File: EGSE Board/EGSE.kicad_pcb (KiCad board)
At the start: 2 copper layers, 149.9 x 112.8 mm, 51 parts, among them J1 DC37_Receptacle, U1 VOR2121A8, U11 DAC121S101, U12 LD1117S33TR_SOT223, U2 VOR2121A8, U3 INA3221, U4 INA238AQDGSRQ1, U5 MAX31865xAP, U6 ISU0205S15, U7 ISO1540, U8 OPA551P, U9 LD1117S33TR_SOT223

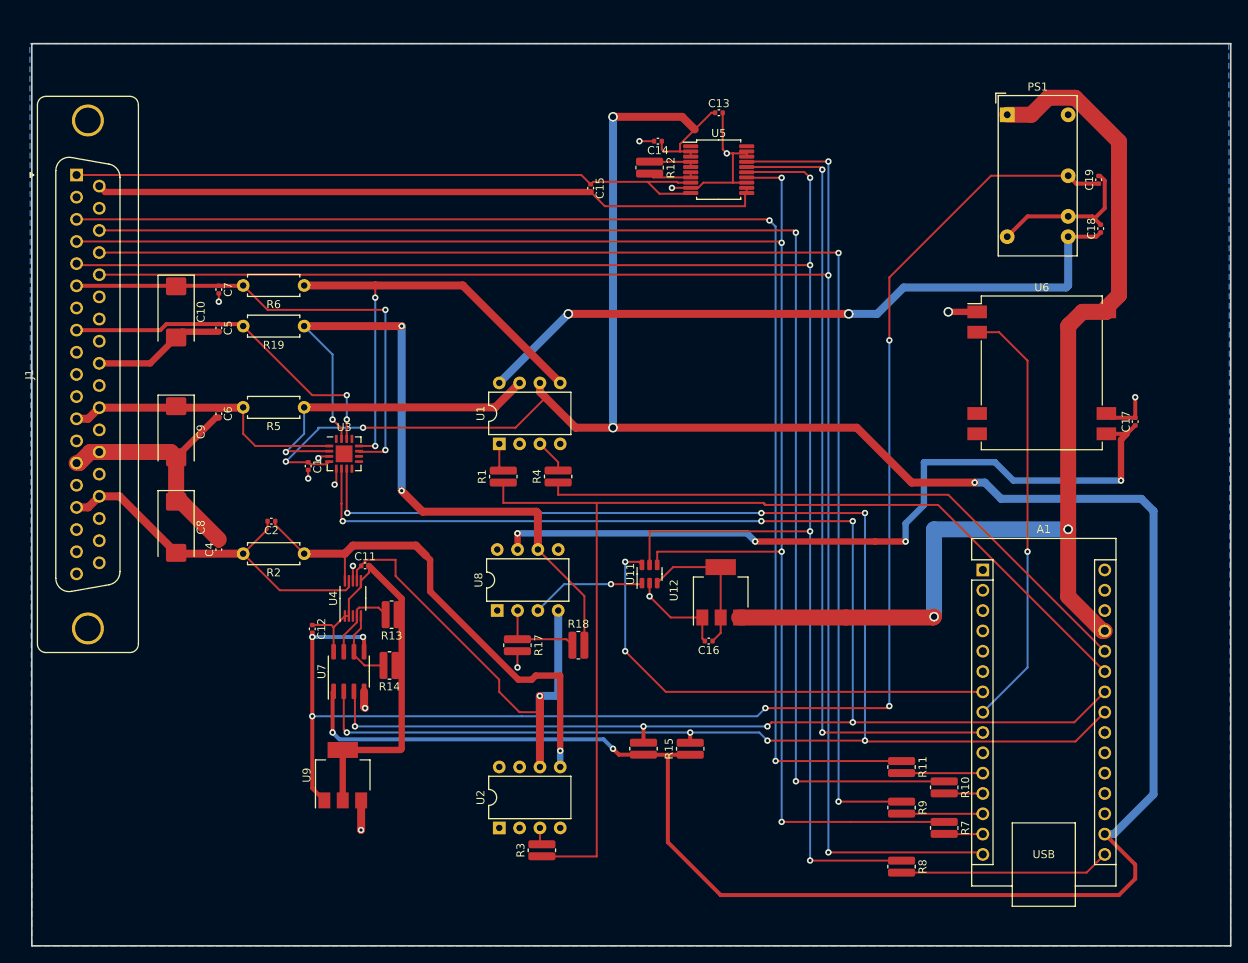
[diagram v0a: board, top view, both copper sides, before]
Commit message: Regular update
Created Gerber files for production
Changed names in arduino code to reflect signal names used by MSSL and on EGSE board
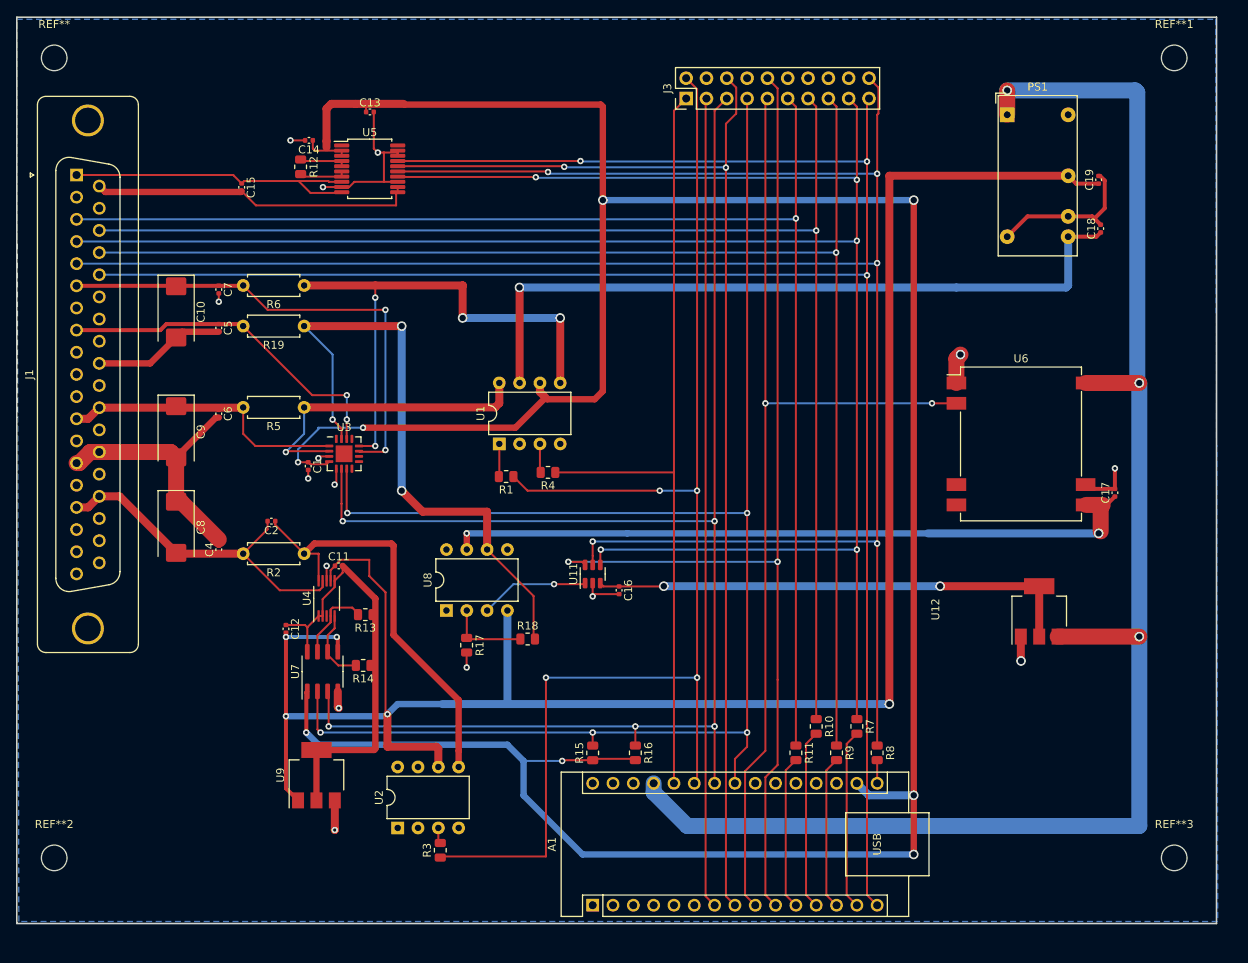
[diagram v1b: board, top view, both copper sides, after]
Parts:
- added J3: Conn_02x10_Odd_Even, Connector_PinHeader_2.54mm:PinHeader_2x10_P2.54mm_Vertical, F.Cu at (103.1, 45.5)
- added REF**: MountingHole_3.2mm_M3, MountingHole:MountingHole_3.2mm_M3, F.Cu at (24.1, 40.4)
- added REF**1: MountingHole_3.2mm_M3, MountingHole:MountingHole_3.2mm_M3, F.Cu at (164.1, 40.4)
- added REF**2: MountingHole_3.2mm_M3, MountingHole:MountingHole_3.2mm_M3, F.Cu at (24.1, 140.4)
- added REF**3: MountingHole_3.2mm_M3, MountingHole:MountingHole_3.2mm_M3, F.Cu at (164.1, 140.4)
- R1, R10, R11, R12, R13, R14, R15, R16, R17, R18, R3, R4, R7, R8, R9: footprint Resistor_SMD:R_0612_1632Metric -> Resistor_SMD:R_0805_2012Metric
- moved A1 64.3 mm to (91.4, 146.3), turned to 90 degrees
- moved C15 43.6 mm to (47.6, 56.6)
- moved R12 43.6 mm to (54.9, 54.0)
- moved C14 43.6 mm to (56.0, 50.7)
- moved U5 43.6 mm to (63.6, 54.3)
- moved C13 43.6 mm to (63.6, 47.1)
- moved U12 39.9 mm to (147.3, 109.6)
- moved R10 17.7 mm to (119.4, 124.0)
- moved R7 16.7 mm to (124.5, 124.0)
- moved R8 14.5 mm to (127.0, 127.3)
- moved R11 13.3 mm to (116.8, 127.3)
- moved C16 12.9 mm to (94.7, 106.9), turned to -90 degrees
- moved R3 12.7 mm to (72.4, 139.4)
- moved U2 12.7 mm to (67.1, 136.6)
- moved R15 12.2 mm to (91.4, 127.3)
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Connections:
- A1 pad 10: /TRIG -> /HTR_DAC_CS
- A1 pad 7: /HTR_DAC_CS -> /TRIG
- A1 pad 8: /HTR_EN -> /RTD_MON_CS
- A1 pad 9: /RTD_MON_CS -> /HTR_EN
- C18 pad 1: Net-(PS1-+Vout) -> /PowerSupplies/+12V_Unswitched
- PS1 pad 6: Net-(PS1-+Vout) -> /PowerSupplies/+12V_Unswitched
- R5 pad 1: Net-(U1-S1') -> Net-(U1-S1)
- U1 pad 7: Net-(U1-S1') -> /PowerSupplies/+12V_Unswitched
- U1 pad 8: Net-(PS1-+Vout) -> Net-(U1-S1)
- U3 pad 2: Net-(U1-S1') -> Net-(U1-S1)
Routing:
- net /TRIG: track 0.00 -> 101.3 mm
- net /PowerSupplies/+12V_Unswitched: track 0.00 -> 91.0 mm, vias 0 -> 1
- net Net-(PS1-+Vout): track 86.5 -> 0.00 mm, vias 2 -> 0
- net /HTR_DAC_CS: track 60.2 -> 133.5 mm
- net /HTR_EN: track 54.0 -> 126.4 mm, vias 1 -> 2
- net /DETEC_SCK: track 221.1 -> 282.7 mm, vias 4 -> 5
- net /DETEC_MOSI: track 210.6 -> 267.1 mm, vias 4 -> 5
- net +5V: track 136.8 -> 191.9 mm, vias 2 -> 3
- net /DETEC_MISO: track 207.1 -> 256.2 mm
- net /RTD_MON_CS: track 100.0 -> 146.0 mm
- net /DETEC_TRP: track 83.5 -> 39.8 mm
- net /DETEC_TRP_RTN: track 84.1 -> 40.6 mm
- net Net-(U11B-+V_A): track 18.4 -> 61.3 mm, vias 0 -> 2
- net Net-(U1-S1'): track 40.2 -> 0.00 mm, vias 1 -> 0
- net Net-(U1-S1): track 0.00 -> 39.1 mm, vias 0 -> 1
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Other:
- board size 149.9 x 112.8 mm -> 150 x 113.3 mm

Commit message: PCB Second draft
Final PCB and Gerber files for production
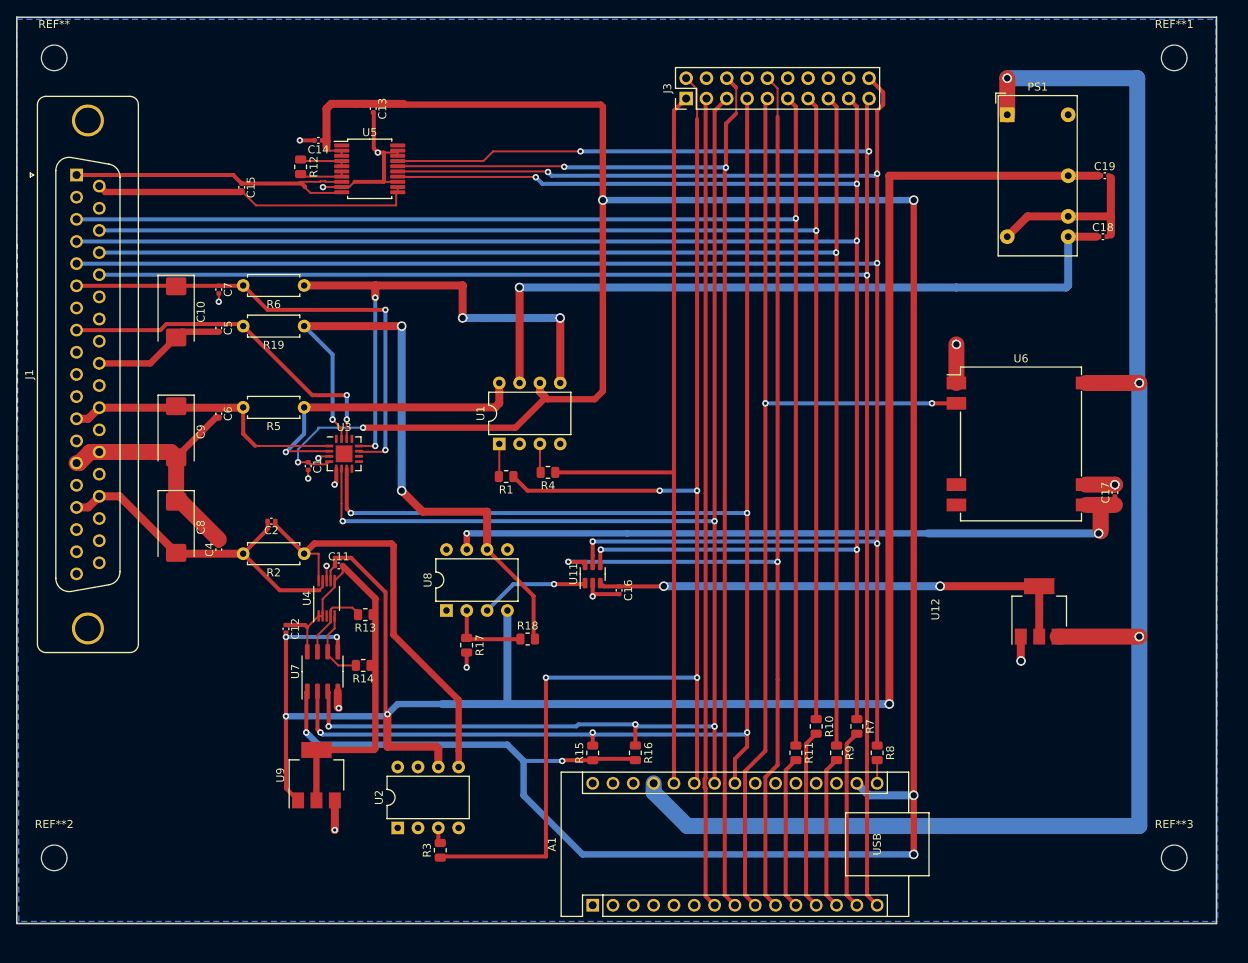
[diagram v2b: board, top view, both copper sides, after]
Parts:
- moved C14 1.17 mm to (57.1, 50.7)
- moved C18 1.05 mm to (155.2, 62.7), turned to 0 degrees
- moved C19 0.92 mm to (155.4, 55.1), turned to 0 degrees
- moved C13 0.58 mm to (64.0, 46.7), turned to -90 degrees
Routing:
- net +3.3V: track 363.4 -> 359.7 mm
- net +5V: track 191.9 -> 195.1 mm
- net /BoardHeater/+15V: track 88.8 -> 87.3 mm
- net /DETEC_MISO: track 256.2 -> 257.1 mm
- net /-12V_UNSWITCHED: track 253.4 -> 252.6 mm
- net /PowerSupplies/+12V_Unswitched: track 91.0 -> 90.3 mm
- net /DETEC_SCK: track 282.7 -> 283.4 mm
